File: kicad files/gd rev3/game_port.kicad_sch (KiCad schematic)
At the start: 41 parts, among them J11 Game Port, Q4 BC817, Q5 BC817, Q6 BC817, Q7 BC817, U18 HCT251, U20 NE556, U21 NE556

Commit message: ERC clean-up
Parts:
- C53, C70, C73, C74: footprint Capacitor_SMD:C_0603_1608Metric -> Capacitor_SMD:C_0805_2012Metric
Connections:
- net C060-67 renamed ~{C060-67}
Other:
- moved on the sheet: R73, R74

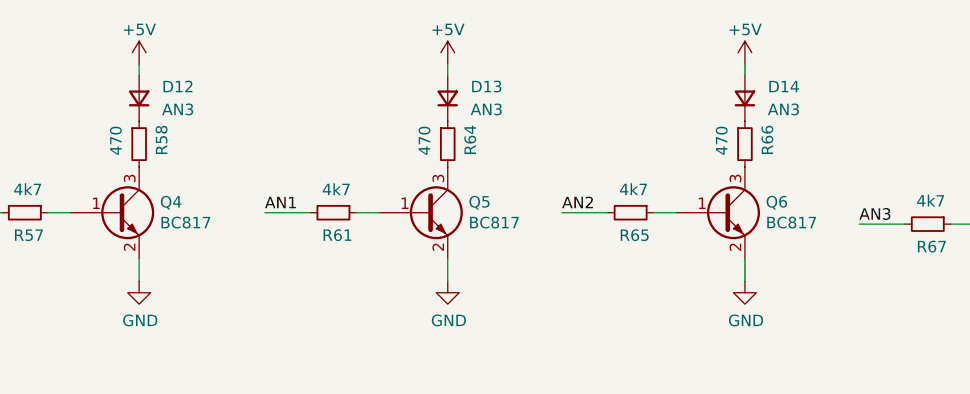
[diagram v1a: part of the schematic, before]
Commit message: colorized multi-sheet, other minor changes
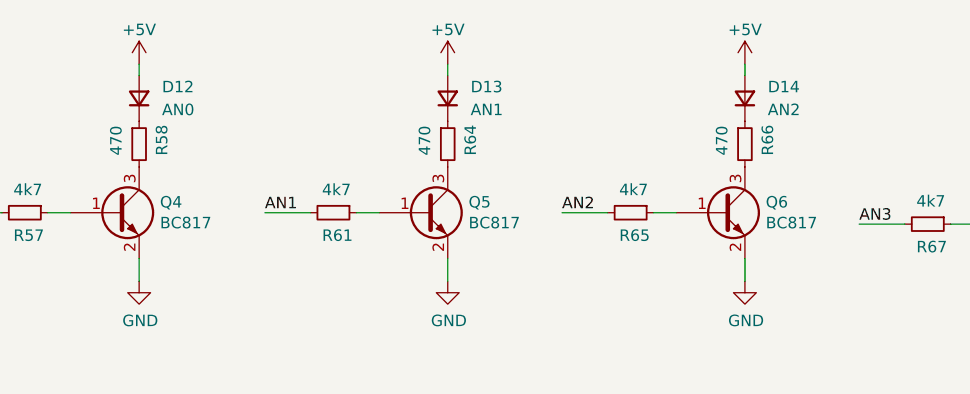
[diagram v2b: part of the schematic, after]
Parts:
- D12: value AN3 -> AN0
- D13: value AN3 -> AN1
- D14: value AN3 -> AN2
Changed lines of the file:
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@@
       (effects (font (size 1.27 1.27)) (justify right))
     )
-    (property "Value" "AN3" (id 1) (at 167.64 40.6399 90)
+    (property "Value" "AN0" (id 1) (at 167.64 40.6399 90)
       (effects (font (size 1.27 1.27)) (justify right))
     )
@@
       (effects (font (size 1.27 1.27)) (justify right))
     )
-    (property "Value" "AN3" (id 1) (at 234.95 40.6399 90)
+    (property "Value" "AN2" (id 1) (at 234.95 40.6399 90)
       (effects (font (size 1.27 1.27)) (justify right))
     )
@@
       (effects (font (size 1.27 1.27)) (justify right))
     )
-    (property "Value" "AN3" (id 1) (at 201.93 40.6399 90)
+    (property "Value" "AN1" (id 1) (at 201.93 40.6399 90)
       (effects (font (size 1.27 1.27)) (justify right))
     )

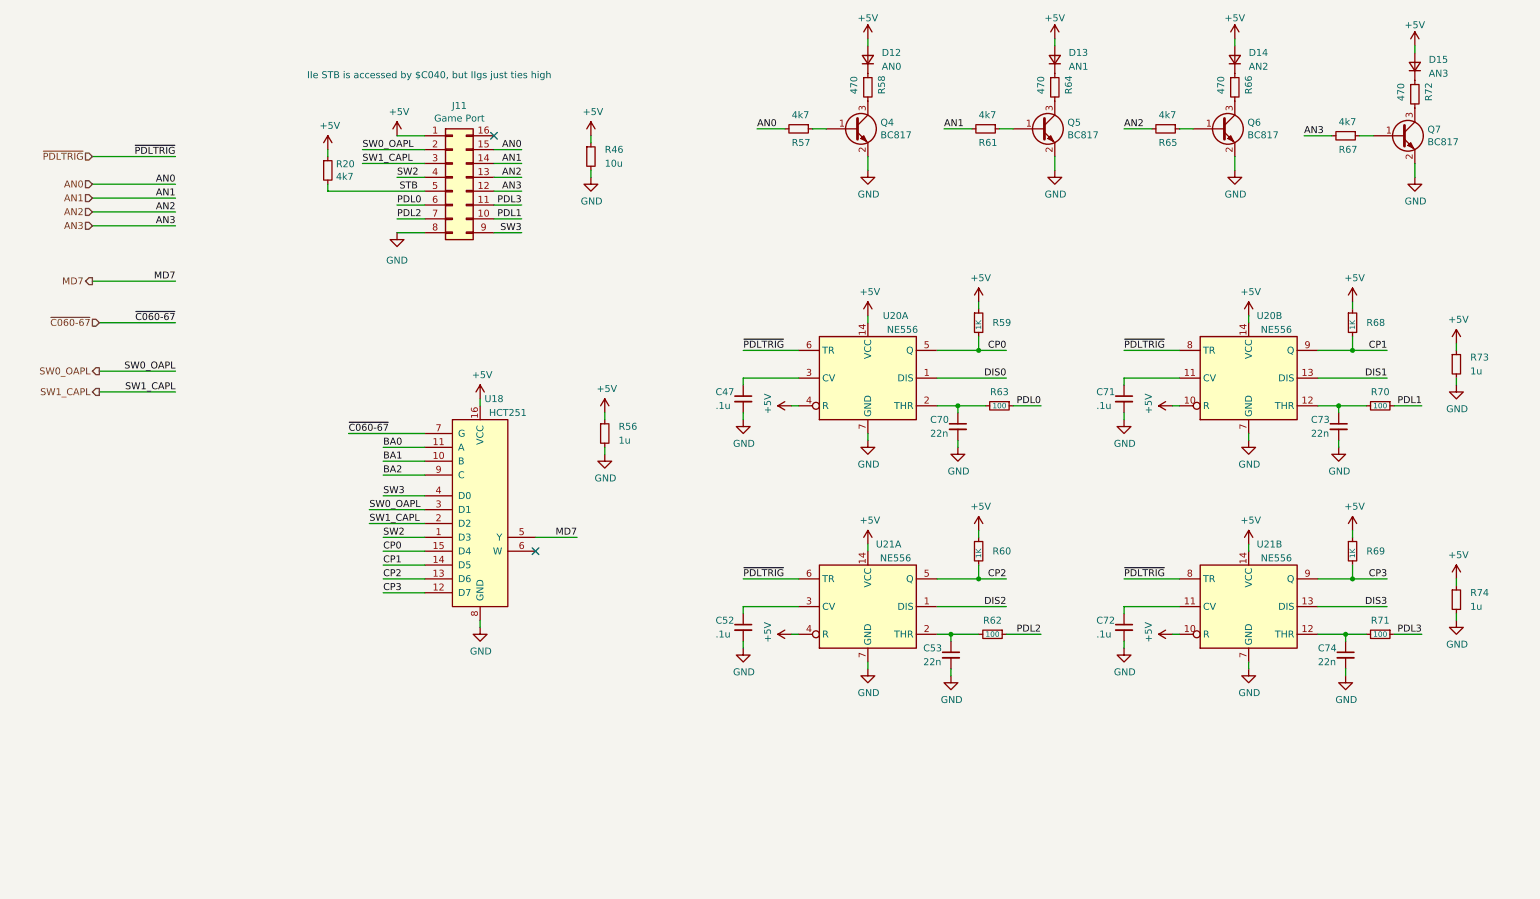
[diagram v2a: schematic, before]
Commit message: main grouping done now optimizing groups and locations
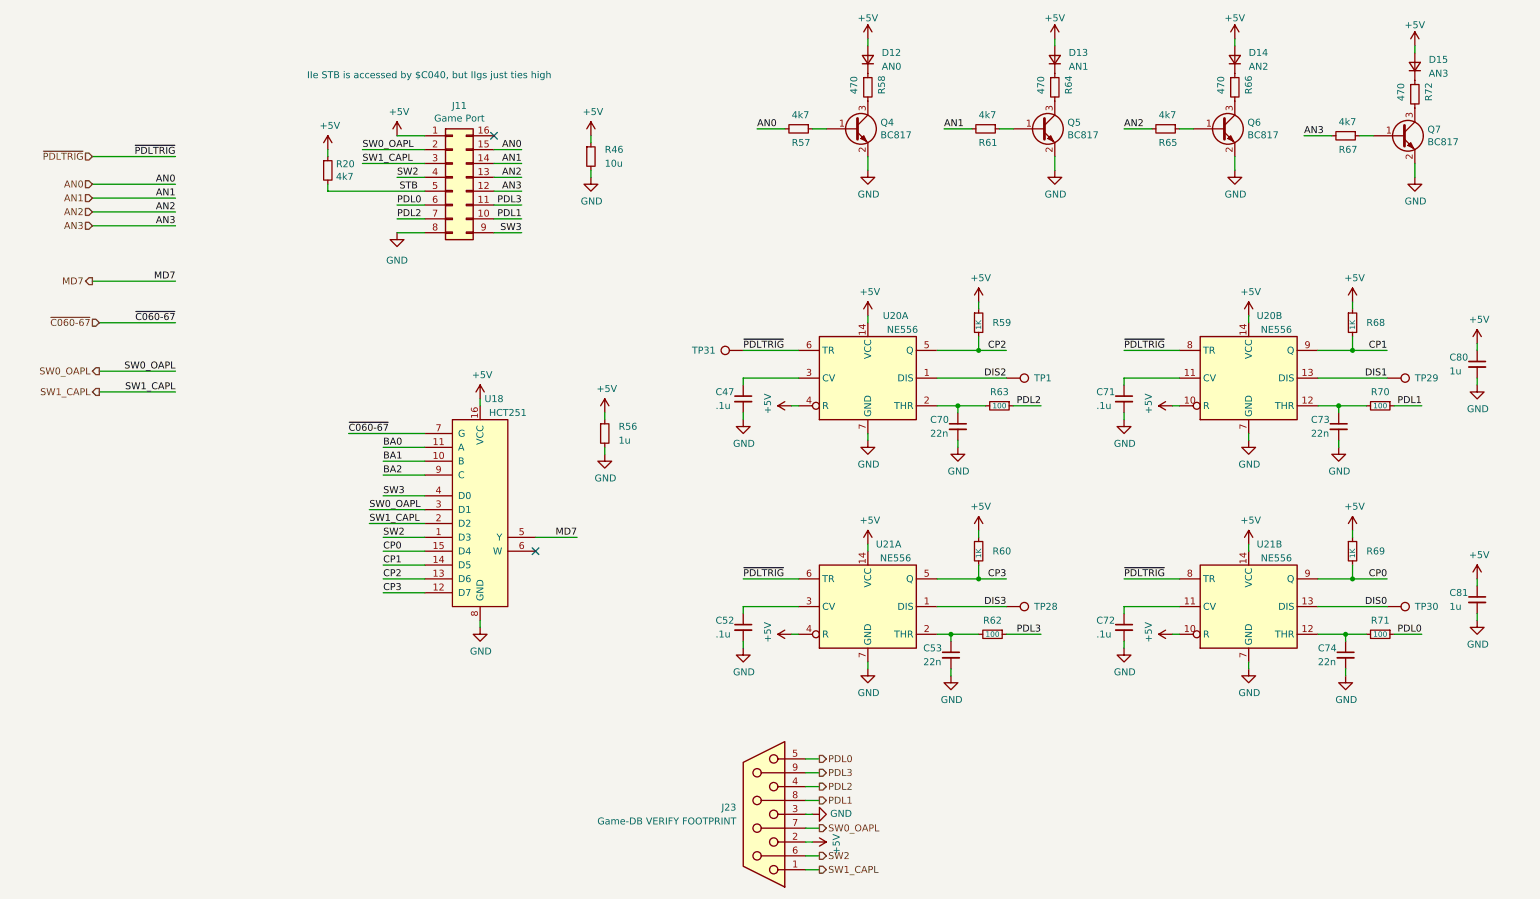
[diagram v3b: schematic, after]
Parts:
- removed R73, R74: 1u, Resistor_SMD:R_0805_2012Metric, symbol My Library:R_0805
- added C80, C81: 1u, Capacitor_SMD:C_0805_2012Metric, symbol My_Library:C_0805
- added J23: Game-DB VERIFY FOOTPRINT, Connector_Dsub:DSUB-9_Female_Horizontal_P2.77x2.84mm_EdgePinOffset4.94mm_Housed_MountingHolesOffset7.48mm, symbol Connector:DB9_Female
- added TP1, TP28, TP29, TP30, TP31: TestPoint, TestPoint:TestPoint_Pad_D1.0mm, symbol Connector:TestPoint
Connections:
- net +5V: now also C80.1, C81.1, J23.2
- net CP0: now also R69.2, U21.9 (Q); no longer R59.2, U20.5 (Q)
- net CP2: now also R59.2, U20.5 (Q); no longer R60.2, U21.5 (Q)
- net CP3: now also R60.2, U21.5 (Q); no longer R69.2, U21.9 (Q)
- net DIS0: now also U21.13 (DIS), TP30.1; no longer U20.1 (DIS)
- net DIS1: now also TP29.1
- net DIS2: now also U20.1 (DIS), TP1.1; no longer U21.1 (DIS)
- net DIS3: now also U21.1 (DIS), TP28.1; no longer U21.13 (DIS)
- net GND: now also C80.2, C81.2, J23.3
- net PDL0: now also R71.1, J23.5; no longer R63.1
- net PDL1: now also J23.8
- net PDL2: now also R63.1, J23.4; no longer R62.1
- net PDL3: now also R62.1, J23.9; no longer R71.1
- net SW0_OAPL: now also J23.7
- net SW1_CAPL: now also J23.1
- net SW2: now also J23.6
- net ~{PDLTRIG}: now also TP31.1

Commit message: added 9-pin gameport based on Bit Preserve IIe schematic
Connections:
- net CP0: now also R60.2, U21.5 (Q); no longer R69.2, U21.9 (Q)
- net CP2: now also R69.2, U21.9 (Q); no longer R59.2, U20.5 (Q)
- net CP3: now also R59.2, U20.5 (Q); no longer R60.2, U21.5 (Q)
- net DIS0: now also TP28.1, U21.1 (DIS); no longer TP30.1, U21.13 (DIS)
- net DIS2: now also TP30.1, U21.13 (DIS); no longer TP1.1, U20.1 (DIS)
- net DIS3: now also TP1.1, U20.1 (DIS); no longer TP28.1, U21.1 (DIS)
- net PDL0: now also R62.1; no longer R71.1
- net PDL2: now also R71.1; no longer R63.1
- net PDL3: now also R63.1; no longer R62.1
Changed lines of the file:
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@@
     (effects (font (size 1.27 1.27)) (justify left bottom))
   )
-  (label "DIS0" (at 260.35 139.7 180)
+  (label "DIS0" (at 190.5 139.7 180)
     (effects (font (size 1.27 1.27)) (justify right bottom))
   )
@@
     (effects (font (size 1.27 1.27)) (justify right bottom))
   )
-  (label "PDL0" (at 266.7 144.78 180)
+  (label "PDL0" (at 196.85 144.78 180)
     (effects (font (size 1.27 1.27)) (justify right bottom))
   )
@@
     (effects (font (size 1.27 1.27)) (justify left bottom))
   )
-  (label "PDL2" (at 196.85 102.87 180)
+  (label "PDL2" (at 266.7 144.78 180)
     (effects (font (size 1.27 1.27)) (justify right bottom))
   )
@@
     (effects (font (size 1.27 1.27)) (justify right bottom))
   )
-  (label "DIS3" (at 190.5 139.7 180)
+  (label "DIS3" (at 190.5 97.79 180)
     (effects (font (size 1.27 1.27)) (justify right bottom))
   )
-  (label "CP3" (at 190.5 134.62 180)
+  (label "CP3" (at 190.5 92.71 180)
     (effects (font (size 1.27 1.27)) (justify right bottom))
   )
@@
     (effects (font (size 1.27 1.27)) (justify right bottom))
   )
-  (label "CP0" (at 260.35 134.62 180)
+  (label "CP0" (at 190.5 134.62 180)
     (effects (font (size 1.27 1.27)) (justify right bottom))
   )
@@
     (effects (font (size 1.27 1.27)) (justify left bottom))
   )
-  (label "CP2" (at 190.5 92.71 180)
+  (label "CP2" (at 260.35 134.62 180)
     (effects (font (size 1.27 1.27)) (justify right bottom))
   )
@@
     (effects (font (size 1.27 1.27)) (justify left bottom))
   )
-  (label "DIS2" (at 190.5 97.79 180)
+  (label "DIS2" (at 260.35 139.7 180)
     (effects (font (size 1.27 1.27)) (justify right bottom))
   )
@@
     (effects (font (size 1.27 1.27)) (justify right bottom))
   )
-  (label "PDL3" (at 196.85 144.78 180)
+  (label "PDL3" (at 196.85 102.87 180)
     (effects (font (size 1.27 1.27)) (justify right bottom))
   )

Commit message: stream cleanup
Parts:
- removed R46: 10u, Resistor_SMD:R_0805_2012Metric, symbol My Library:R_0805
- removed R56: 1u, Resistor_SMD:R_0805_2012Metric, symbol My Library:R_0805
- added C83: 10u, Capacitor_SMD:C_0805_2012Metric, symbol My_Library:C_0805
- added C84: 1u, Capacitor_SMD:C_0805_2012Metric, symbol My_Library:C_0805
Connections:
- net +5V: now also C83.1, C84.1
- net GND: now also C83.2, C84.2
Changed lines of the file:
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@@
-    (pin "2")
-  )
-  (symbol (lib_id "My Library:R_0805") (at 116.84 107.95 0) (unit 1)
-    (in_bom yes) (on_board yes) (fields_autoplaced)
-    (property "Reference" "R56" (id 0) (at 119.38 106.6799 0)
-      (effects (font (size 1.27 1.27)) (justify left))
-    )
-    (property "Value" "1u" (id 1) (at 119.38 109.2199 0)
-      (effects (font (size 1.27 1.27)) (justify left))
-    )
-    (property "Footprint" "Resistor_SMD:R_0805_2012Metric" (id 2) (at 116.84 107.95 0)
-      (effects (font (size 1.27 1.27)) hide)
-    )
-    (property "Datasheet" "~" (id 3) (at 116.84 107.95 0)
-      (effects (font (size 1.27 1.27)) hide)
-    )
-    (pin "1")
     (pin "2")
   )
@@
     (pin "2")
   )
-  (symbol (lib_id "My Library:R_0805") (at 114.3 57.15 0) (unit 1)
-    (in_bom yes) (on_board yes) (fields_autoplaced)
-    (property "Reference" "R46" (id 0) (at 116.84 55.8799 0)
-      (effects (font (size 1.27 1.27)) (justify left))
-    )
-    (property "Value" "10u" (id 1) (at 116.84 58.4199 0)
-      (effects (font (size 1.27 1.27)) (justify left))
-    )
-    (property "Footprint" "Resistor_SMD:R_0805_2012Metric" (id 2) (at 114.3 57.15 0)
-      (effects (font (size 1.27 1.27)) hide)
-    )
-    (property "Datasheet" "~" (id 3) (at 114.3 57.15 0)
-      (effects (font (size 1.27 1.27)) hide)
-    )
-    (pin "1")
-    (pin "2")
-  )
   (symbol (lib_id "power:+5V") (at 165.1 35.56 0) (unit 1)
     (in_bom yes) (on_board yes)
@@
     (pin "1")
   )
+  (symbol (lib_name "C_0805_5") (lib_id "My_Library:C_0805") (at 116.84 107.95 0) (unit 1)
+    (in_bom yes) (on_board yes)
+    (property "Reference" "C84" (id 0) (at 111.76 106.68 0)
+      (effects (font (size 1.27 1.27)) (justify left))
+    )
+    (property "Value" "1u" (id 1) (at 111.76 109.22 0)
+      (effects (font (size 1.27 1.27)) (justify left))
+    )
+    (property "Footprint" "Capacitor_SMD:C_0805_2012Metric" (id 2) (at 116.84 107.95 0)
+      (effects (font (size 1.27 1.27)) hide)
+    )
+    (property "Datasheet" "~" (id 3) (at 116.84 107.95 0)
+      (effects (font (size 1.27 1.27)) hide)
+    )
+    (pin "1")
+    (pin "2")
+  )
   (symbol (lib_name "R_0805_5") (lib_id "My_Library:R_0805") (at 219.71 52.07 270) (unit 1)
     (in_bom yes) (on_board yes)
@@
     (pin "1")
   )
+  (symbol (lib_name "C_0805_5") (lib_id "My_Library:C_0805") (at 114.3 57.15 0) (unit 1)
+    (in_bom yes) (on_board yes)
+    (property "Reference" "C83" (id 0) (at 109.22 55.88 0)
+      (effects (font (size 1.27 1.27)) (justify left))
+    )
+    (property "Value" "10u" (id 1) (at 109.22 58.42 0)
+      (effects (font (size 1.27 1.27)) (justify left))
+    )
+    (property "Footprint" "Capacitor_SMD:C_0805_2012Metric" (id 2) (at 114.3 57.15 0)
+      (effects (font (size 1.27 1.27)) hide)
+    )
+    (property "Datasheet" "~" (id 3) (at 114.3 57.15 0)
+      (effects (font (size 1.27 1.27)) hide)
+    )
+    (pin "1")
+    (pin "2")
+  )
   (symbol (lib_id "power:GND") (at 114.3 60.96 0) (unit 1)

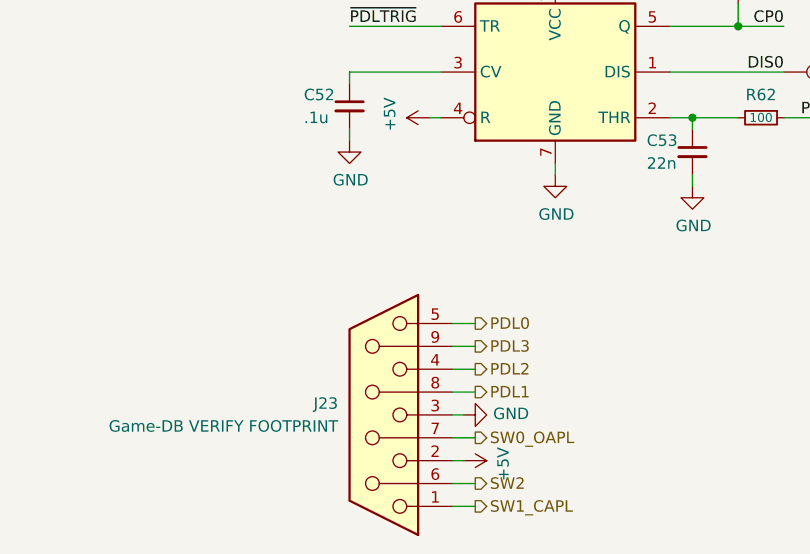
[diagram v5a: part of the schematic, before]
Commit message: Rough routing Main Data to figure out PCB floorplan.
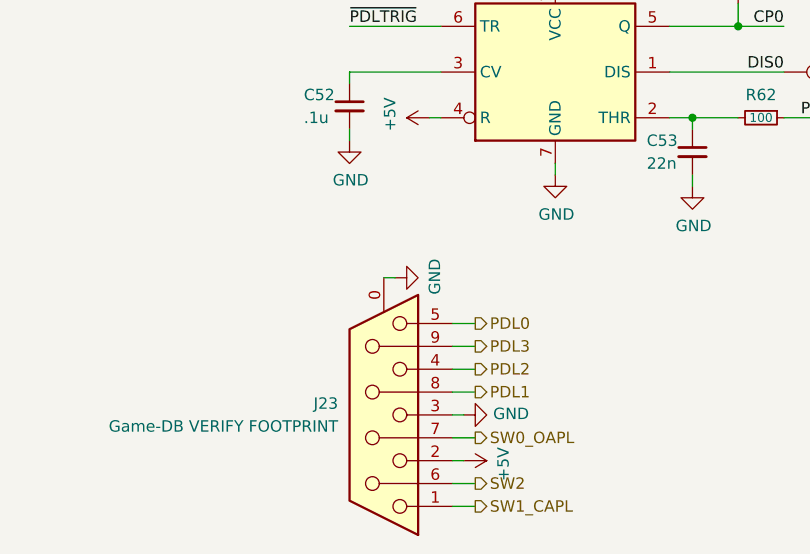
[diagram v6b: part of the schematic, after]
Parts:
- J23: symbol Connector:DB9_Female -> Connector:DB9_Female_MountingHoles
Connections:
- net GND: now also J23.0 (PAD)
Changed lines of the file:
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@@
+    (stroke (width 0) (type default) (color 0 0 0 0))
+  )
+  (wire (pts (xy 146.05 162.56) (xy 147.32 162.56))
     (stroke (width 0) (type default) (color 0 0 0 0))
   )
@@
     (pin "2")
   )
-  (symbol (lib_id "Connector:DB9_Female") (at 146.05 177.8 180) (unit 1)
+  (symbol (lib_id "Connector:DB9_Female_MountingHoles") (at 146.05 177.8 180) (unit 1)
     (in_bom yes) (on_board yes) (fields_autoplaced)
     (property "Reference" "J23" (id 0) (at 140.97 176.5299 0)
@@
       (effects (font (size 1.27 1.27)) hide)
     )
+    (pin "0")
     (pin "1")
     (pin "2")
@@
       (effects (font (size 1.27 1.27)) hide)
     )
+    (pin "1")
+  )
+  (symbol (lib_id "power:GND") (at 147.32 162.56 90) (unit 1)
+    (in_bom yes) (on_board yes)
+    (property "Reference" "#PWR0401" (id 0) (at 153.67 162.56 0)
+      (effects (font (size 1.27 1.27)) hide)
+    )
+    (property "Value" "GND" (id 1) (at 151.7142 162.433 0))
+    (property "Footprint" "" (id 2) (at 147.32 162.56 0)
+      (effects (font (size 1.27 1.27)) hide)
+    )
+    (property "Datasheet" "" (id 3) (at 147.32 162.56 0)
+      (effects (font (size 1.27 1.27)) hide)
+    )
